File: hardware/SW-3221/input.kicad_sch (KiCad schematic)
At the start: 38 parts, among them J8 MIC, J9 LINE_IN, SW3 PEC11R-4225F-50024, SW4 DNP, SW5 DNP, U5 Opamp_Quad

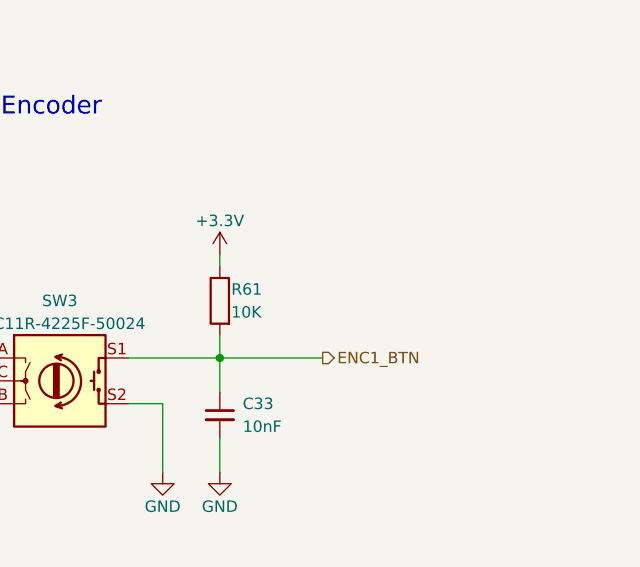
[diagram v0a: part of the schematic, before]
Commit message: use io5 for encoder switch
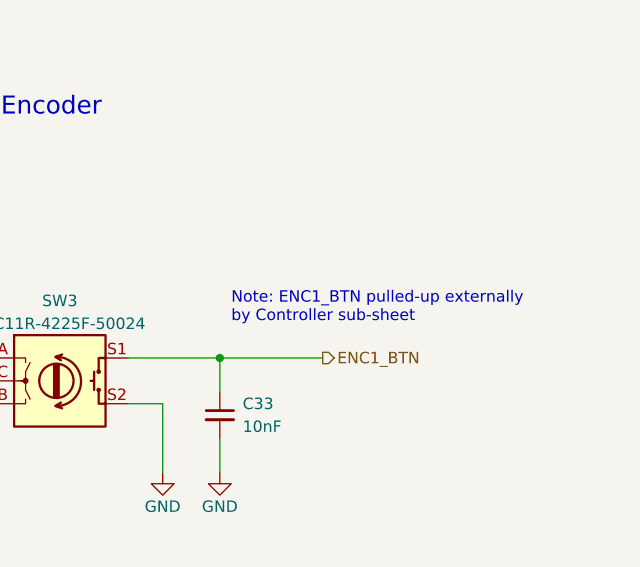
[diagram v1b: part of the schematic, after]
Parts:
- removed R61: 10K, Resistor_SMD:R_0603_1608Metric, symbol Device:R
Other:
- note added: "Note: ENC1_BTN pulled-up externally by Controller sub-sheet"
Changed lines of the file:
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@@
   (title_block
     (title "SW-3221: Front Panel Input")
-    (date "2022-01-31")
+    (date "2022-01-30")
     (rev "1")
   )
@@
     (stroke (width 0) (type default) (color 0 0 0 0))
   )
-  (wire (pts (xy 245.11 41.91) (xy 245.11 43.18))
-    (stroke (width 0) (type default) (color 0 0 0 0))
-  )
   (wire (pts (xy 96.52 124.46) (xy 100.33 124.46))
     (stroke (width 0) (type default) (color 0 0 0 0))
@@
   )
   (wire (pts (xy 200.66 58.42) (xy 200.66 59.69))
-    (stroke (width 0) (type default) (color 0 0 0 0))
-  )
-  (wire (pts (xy 245.11 50.8) (xy 245.11 53.34))
     (stroke (width 0) (type default) (color 0 0 0 0))
   )
@@
   (text "Buttons" (at 256.54 92.71 0)
     (effects (font (size 2 2)) (justify left bottom))
+  )
+  (text "Note: ENC1_BTN pulled-up externally \nby Controller sub-sheet"
+    (at 246.38 49.53 0)
+    (effects (font (size 1.27 1.27)) (justify left bottom))
   )
   (text "Offset: +1.65V\nAV: 100" (at 106.68 72.39 0)
@@
     (pin "1")
   )
-  (symbol (lib_id "Device:R") (at 245.11 46.99 0) (mirror y) (unit 1)
-    (in_bom yes) (on_board yes)
-    (property "Reference" "R61" (id 0) (at 246.38 45.72 0)
-      (effects (font (size 1.27 1.27)) (justify right))
-    )
-    (property "Value" "10K" (id 1) (at 246.38 48.26 0)
-      (effects (font (size 1.27 1.27)) (justify right))
-    )
-    (property "Footprint" "Resistor_SMD:R_0603_1608Metric" (id 2) (at 246.888 46.99 90)
-      (effects (font (size 1.27 1.27)) hide)
-    )
-    (property "Datasheet" "~" (id 3) (at 245.11 46.99 0)
-      (effects (font (size 1.27 1.27)) hide)
-    )
-    (pin "1")
-    (pin "2")
-  )
   (symbol (lib_id "Device:R") (at 76.2 134.62 0) (unit 1)
     (in_bom yes) (on_board yes) (fields_autoplaced)
@@
     (pin "3")
   )
-  (symbol (lib_id "power:+3.3V") (at 245.11 41.91 0) (unit 1)
-    (in_bom yes) (on_board yes)
-    (property "Reference" "#PWR087" (id 0) (at 245.11 45.72 0)
-      (effects (font (size 1.27 1.27)) hide)
-    )
-    (property "Value" "+3.3V" (id 1) (at 245.11 38.1 0))
-    (property "Footprint" "" (id 2) (at 245.11 41.91 0)
-      (effects (font (size 1.27 1.27)) hide)
-    )
-    (property "Datasheet" "" (id 3) (at 245.11 41.91 0)
-      (effects (font (size 1.27 1.27)) hide)
-    )
-    (pin "1")
-  )
   (symbol (lib_id "power:GND") (at 33.02 34.29 0) (unit 1)
